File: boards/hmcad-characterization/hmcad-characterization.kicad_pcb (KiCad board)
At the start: 4 copper layers, 50 parts, among them J1 BARREL, J10 SMA, J11 SMA, J12 CONN_INTEGRALSTICK_FPGA_HOST, J2 SMA, J3 SMA, J4 SMA, J5 SMA, J6 SMA, J7 SMA, J8 SMA, J9 SMA, U1 ASG2-D-X-A-1000.000MHZ, U2 SIT9122AI-2D3-33E625.000000T, U3 PI6C59S6005, U4 LT3042, U5 HMCAD1520

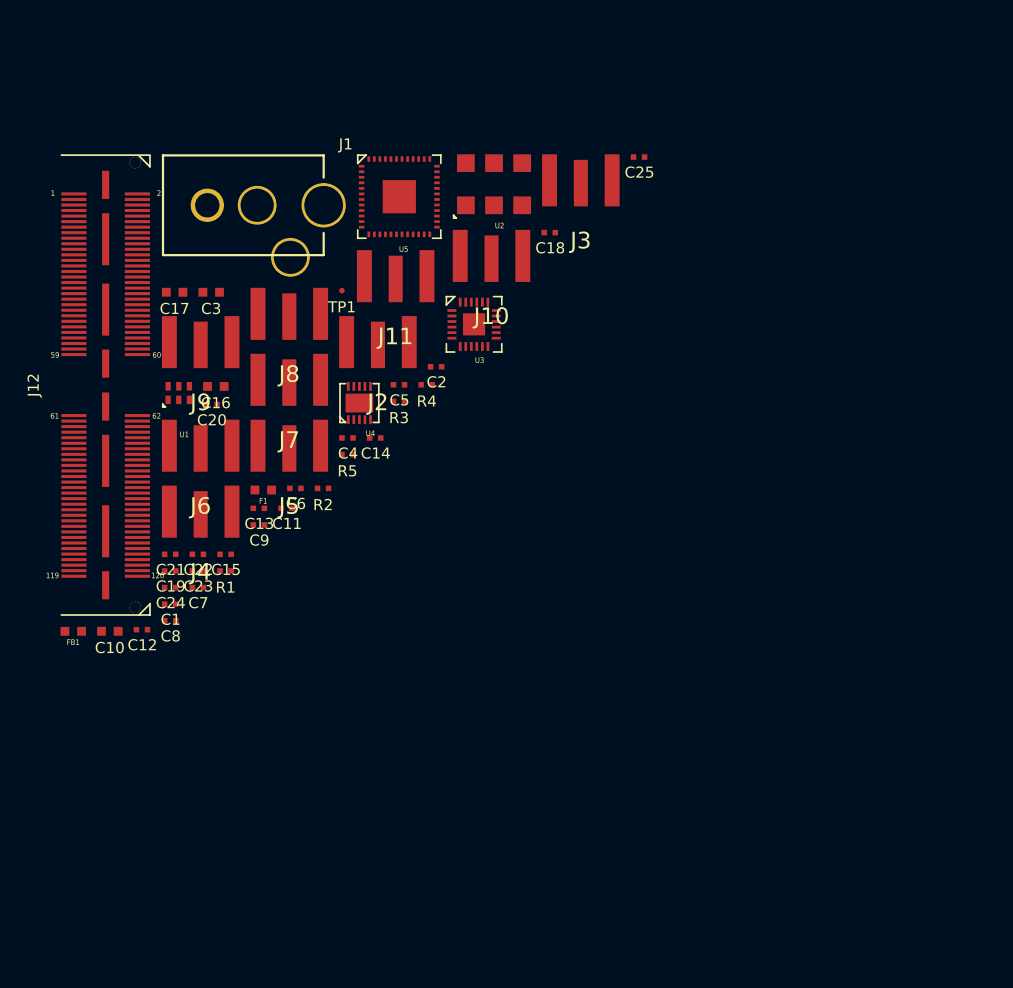
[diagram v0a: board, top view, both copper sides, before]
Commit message: Preliminary layout. Still have to do low speed control lines, power/ground planes, and transitions at SMAs.
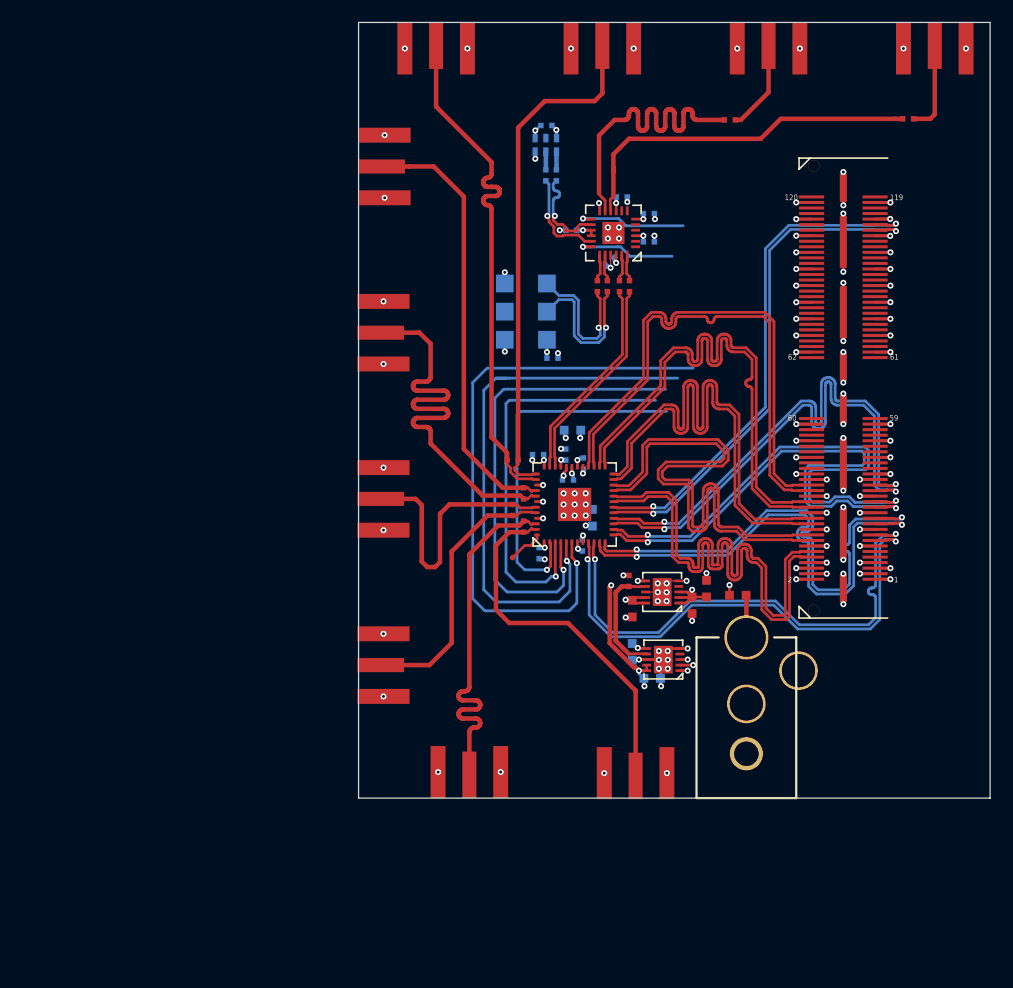
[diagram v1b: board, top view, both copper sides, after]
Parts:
- added C26: 4.7 uF, azonenberg_pcb:EIA_0603_CAP_NOSILK, B.Cu at (103.7, 86.8)
- added C27: 4.7 uF, azonenberg_pcb:EIA_0603_CAP_NOSILK, B.Cu at (105.5, 89.2)
- added U6: LT3042, azonenberg_pcb:DFN_10_0.5MM_3x3MM, F.Cu at (106.5, 87.5)
- C1, C15, C16, C17, C18, C19, C2, C20, C21, C22, C23, C24, C25, C4, C5, C6, C9, U1, U2: moved to B.Cu
- R1: value 33K 1% -> 9.09K 0.1%
- moved C13 68.3 mm to (128.6, 38.7), turned to 180 degrees
- moved J12 66.6 mm to (122.8, 63.0), turned to 180 degrees
- moved J1 63.7 mm to (114.0, 92.0), turned to 90 degrees
- moved FB1 57.3 mm to (110.4, 81.1), turned to 90 degrees
- moved C1 54.9 mm to (96.0, 39.3)
- moved J3 54.3 mm to (89.0, 100.0)
- moved C12 53.8 mm to (103.5, 53.8), turned to 90 degrees
- moved C3 51.8 mm to (109.1, 82.6), turned to 90 degrees
- moved C15 49.0 mm to (105.2, 47.2)
- moved C8 49.0 mm to (100.5, 53.8), turned to 270 degrees
- moved J9 47.8 mm to (101.0, 30.0), turned to 180 degrees
- moved C21 47.7 mm to (101.7, 51.6), turned to 225 degrees
- moved C10 47.2 mm to (103.7, 82.9), turned to 90 degrees
- moved J10 46.4 mm to (131.0, 30.0), turned to 180 degrees
- moved C7 45.9 mm to (101.5, 53.8), turned to 270 degrees
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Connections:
- net Net-(C11-Pad2) renamed /ADC_AC_P
- net Net-(C12-Pad2) renamed /ADC_AC_N
- net Net-(C13-Pad2) renamed /DEBUG_AC_P
- net Net-(C14-Pad2) renamed /DEBUG_AC_N
- net Net-(R1-Pad1) renamed /RSET
- C3 pad 2: Net-(C3-Pad2) -> /3V3_1
- C5 pad 1: /CLK_1GHZ_AC_P -> /CLK_1GHZ_AC_N
- C6 pad 1: /CLK_1GHZ_AC_N -> /CLK_1GHZ_AC_P
- C7 pad 2: /CLK_625MHZ_P -> /CLK_625MHZ_N
- C8 pad 2: /CLK_625MHZ_N -> /CLK_625MHZ_P
- FB1 pad 1: Net-(C3-Pad2) -> /3V3_1
- J12 pad 10: /FCLK_N -> /FCLK_P
- J12 pad 12: /FCLK_P -> /FCLK_N
- J12 pad 15: /LVDS_4B_N -> /LVDS_1A_P
- J12 pad 16: /LVDS_4A_N -> /LVDS_3A_P
- J12 pad 17: /LVDS_4B_P -> /LVDS_1A_N
- J12 pad 18: /LVDS_4A_P -> /LVDS_3A_N
- J12 pad 21: /LVDS_3B_N -> /LVDS_1B_P
- J12 pad 22: /LVDS_3A_N -> /LVDS_3B_P
- J12 pad 23: /LVDS_3B_P -> /LVDS_1B_N
- J12 pad 24: /LVDS_3A_P -> /LVDS_3B_N
- J12 pad 27: /LVDS_2B_N -> /LVDS_2A_P
- J12 pad 28: /LVDS_2A_N -> /LVDS_4A_P
- J12 pad 29: /LVDS_2B_P -> /LVDS_2A_N
- J12 pad 30: /LVDS_2A_P -> /LVDS_4A_N
- J12 pad 33: /LVDS_1B_N -> /LVDS_2B_P
- J12 pad 34: /LVDS_1A_N -> /LVDS_4B_P
- J12 pad 35: /LVDS_1B_P -> /LVDS_2B_N
- J12 pad 36: /LVDS_1A_P -> /LVDS_4B_N
- U4 pad 1: Net-(C3-Pad2) -> /3V3_1
- U4 pad 2: Net-(C3-Pad2) -> /3V3_1
- U4 pad 3: Net-(C3-Pad2) -> /3V3_1
- U4 pad 6: /3V3 -> /3V3_1
- U5 pad PAD: (no net) -> /GND
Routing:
- net /GND: track 0.00 -> 500.9 mm, vias 0 -> 86
- net /3V3: track 0.00 -> 171.9 mm, vias 0 -> 28
- net /1V8: track 0.00 -> 93.9 mm, vias 0 -> 14
- net /ADC_PD: track 0.00 -> 55.8 mm, vias 0 -> 1
- net /A1V8: track 0.00 -> 55.6 mm, vias 0 -> 8
- net /ADC_RST_N: track 0.00 -> 50.1 mm, vias 0 -> 1
- net /IN4_P: track 0.00 -> 47.1 mm
- net /LVDS_2A_N: track 0.00 -> 46.8 mm, vias 0 -> 2
- net /LVDS_4B_P: track 0.00 -> 46.7 mm
- net /LVDS_2A_P: track 0.00 -> 46.7 mm, vias 0 -> 2
- net /LVDS_4A_P: track 0.00 -> 46.7 mm
- net /LCLK_P: track 0.00 -> 46.7 mm, vias 0 -> 2
- net /LCLK_N: track 0.00 -> 46.7 mm, vias 0 -> 2
- net /LVDS_4B_N: track 0.00 -> 46.7 mm
- net /FCLK_N: track 0.00 -> 46.7 mm
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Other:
- board outline added: 57 x 70 mm

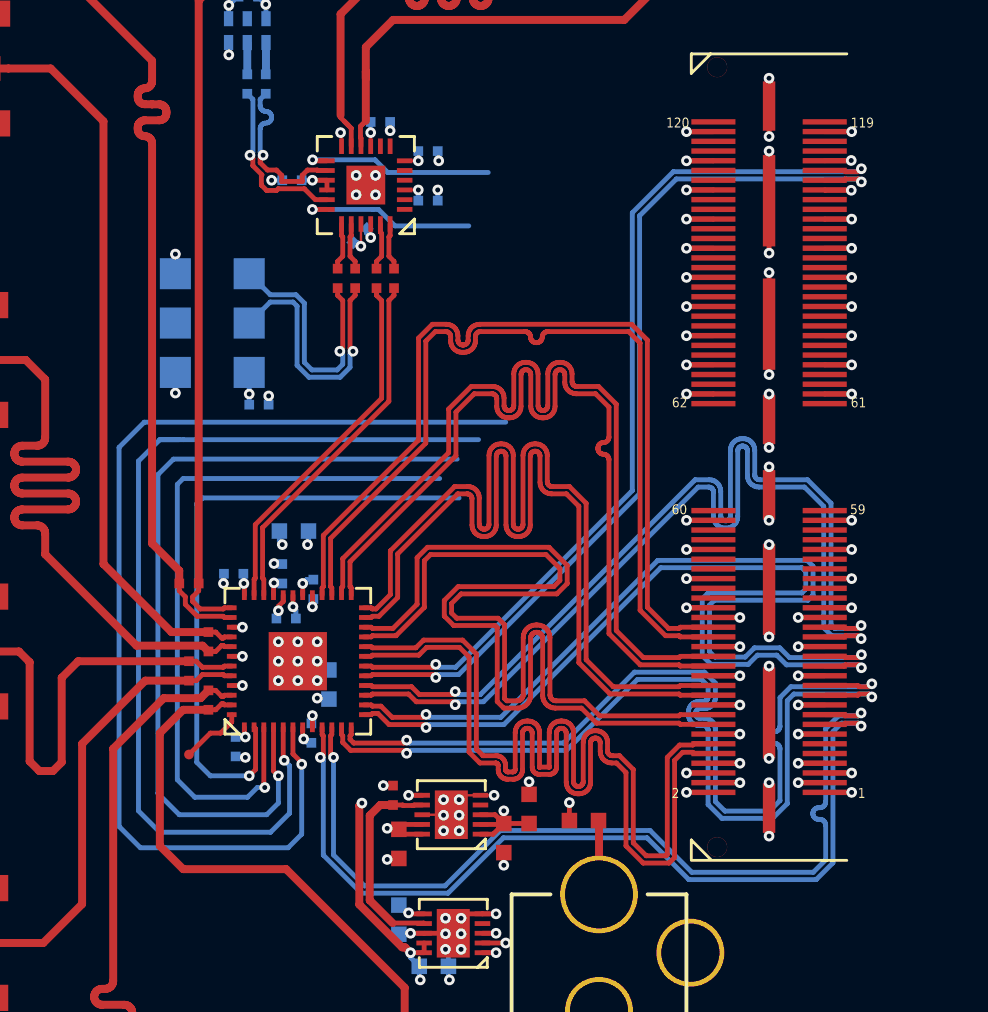
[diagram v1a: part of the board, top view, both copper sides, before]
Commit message: Continued layout on ADC test board. Fixed a bunch of plane crossings.
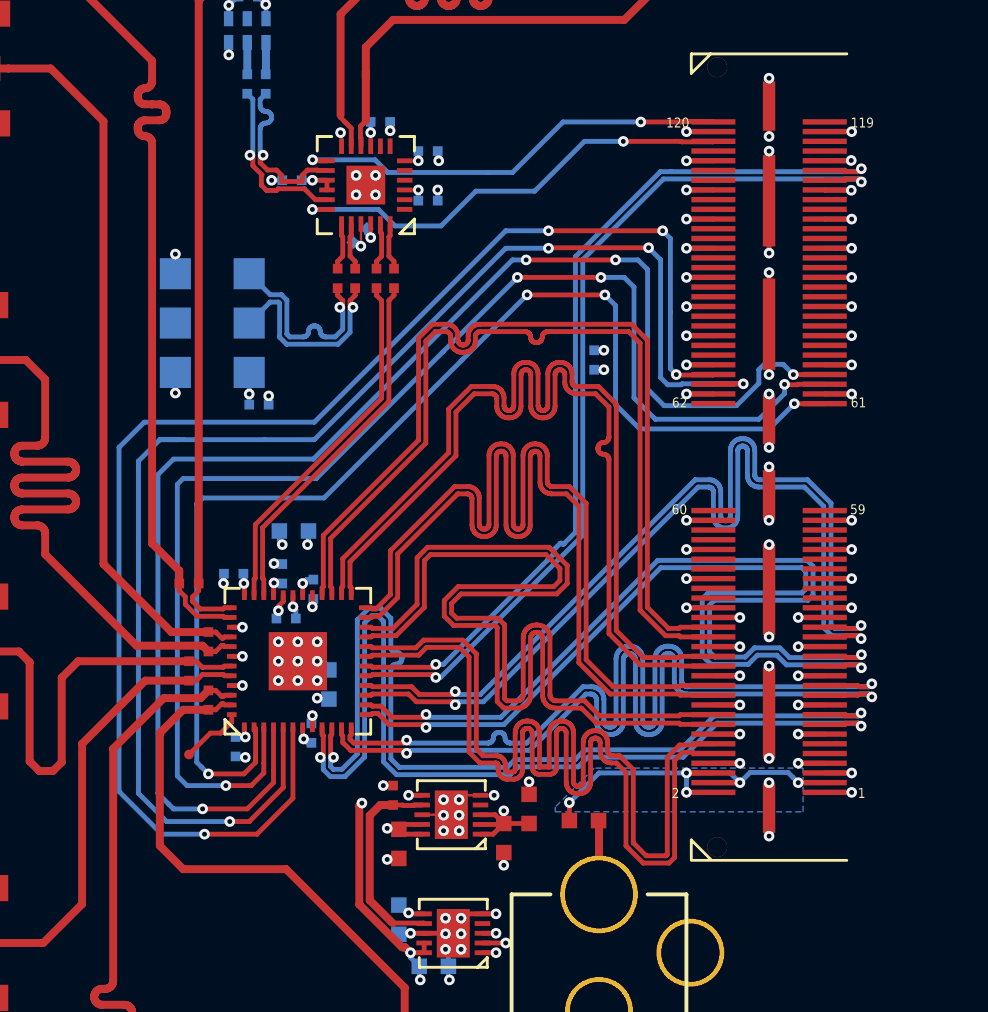
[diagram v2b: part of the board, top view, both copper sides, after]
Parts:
- added C28: 0.47 uF, azonenberg_pcb:EIA_0402_CAP_NOSILK, B.Cu at (113.8, 58.0)
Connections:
- J12 pad 116: (no net) -> /BUF_MUXSEL
- J12 pad 120: (no net) -> /BUF_IN_SEL
- J12 pad 61: (no net) -> /SPI_CS_N
- J12 pad 62: /ADC_PD -> (no net)
- J12 pad 65: /ADC_RST_N -> /SPI_SDATA
- J12 pad 66: /SPI_SCLK -> /ADC_RST_N
- J12 pad 67: /SPI_SDATA -> /SPI_SCLK
- J12 pad 68: /SPI_CS_N -> /ADC_PD
- J12 pad 73: /BUF_MUXSEL -> (no net)
- J12 pad 74: /BUF_IN_SEL -> (no net)
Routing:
- net /SPI_SDATA: track 37.0 -> 67.4 mm, vias 1 -> 4
- net /SPI_SCLK: track 43.0 -> 73.2 mm, vias 1 -> 4
- net /SPI_CS_N: track 32.6 -> 61.8 mm, vias 1 -> 4
- net /ADC_RST_N: track 50.1 -> 73.7 mm, vias 1 -> 4
- net /ADC_PD: track 55.8 -> 74.2 mm, vias 1 -> 4
- net /3V3: track 171.9 -> 187.3 mm, vias 28 -> 29
- net /BUF_MUXSEL: track 9.15 -> 23.6 mm, vias 1 -> 2
- net /BUF_IN_SEL: track 10.1 -> 22.8 mm, vias 1 -> 2
- net /A1V8: track 55.6 -> 51.9 mm
- net /CLK_625MHZ_N: track 13.5 -> 10.3 mm
- net /CLK_625MHZ_P: track 12.9 -> 10.3 mm
- net /LVDS_1A_P: track 46.6 -> 48.6 mm
- net /LVDS_1A_N: track 46.7 -> 48.5 mm
- net /1V8: track 93.9 -> 92.5 mm, vias 14 -> 15
- net /5V0: track 27.9 -> 27.2 mm
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- added copper zone on In2.Cu, net /1V8
- added copper zone on In2.Cu, net /2V5
- added copper zone on In2.Cu, net /3V3
- added copper zone on In2.Cu, net /3V3_1
- added copper zone on B.Cu, net /5V0
- added copper zone on In2.Cu, net /5V0
- added copper zone on In2.Cu, net /A1V8
- added copper zone on In1.Cu, net /GND

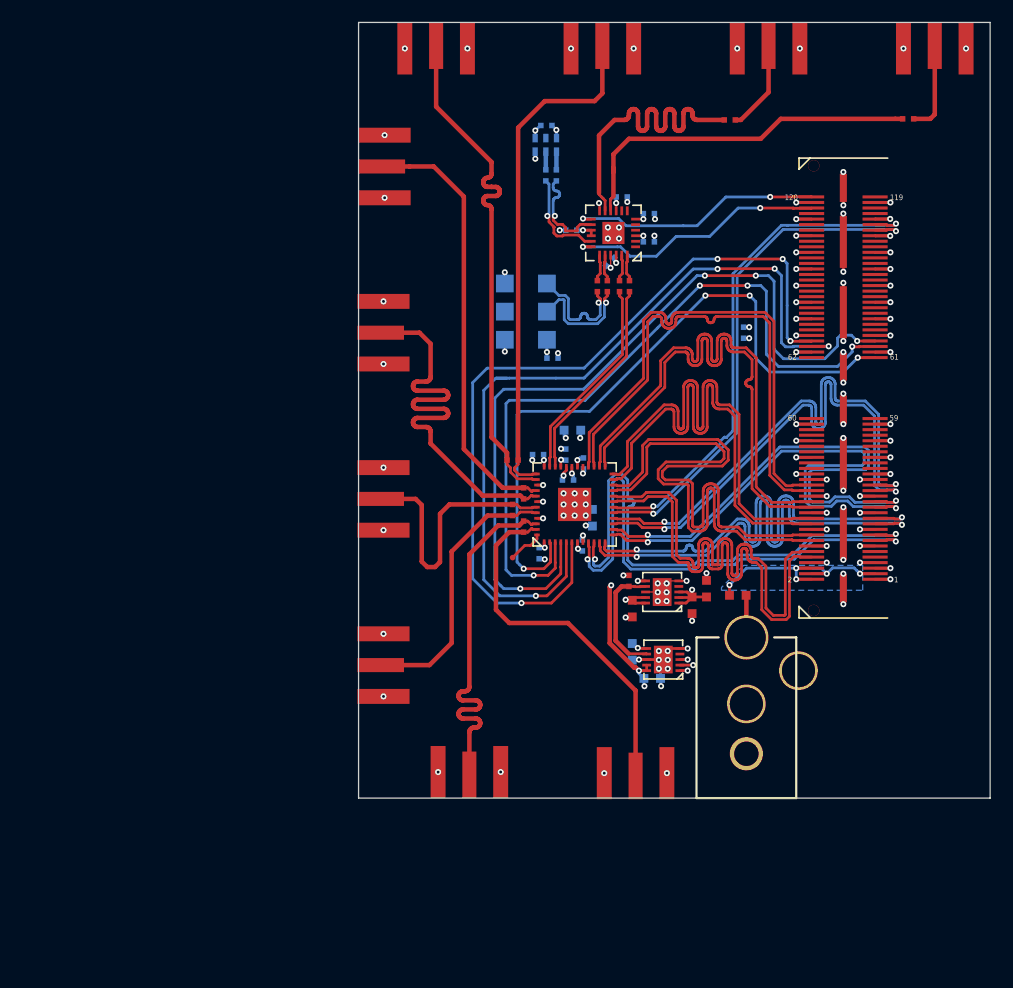
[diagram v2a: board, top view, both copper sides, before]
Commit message: Additional routing tweaks, added soldermask cutouts over RF traces
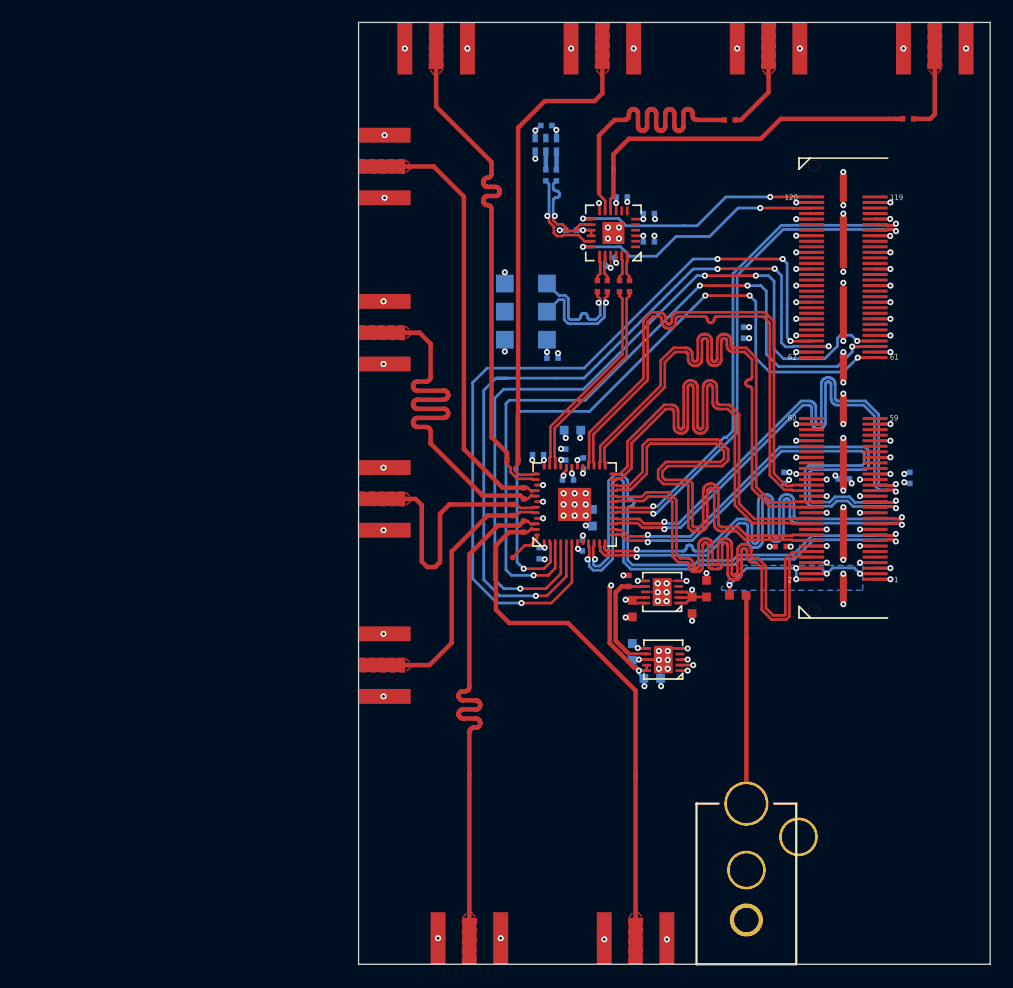
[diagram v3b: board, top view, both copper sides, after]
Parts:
- added C29: 0.47 uF, azonenberg_pcb:EIA_0402_CAP_NOSILK, B.Cu at (117.4, 71.1)
- added C30: 0.47 uF, azonenberg_pcb:EIA_0402_CAP_NOSILK, B.Cu at (122.8, 71.2)
- added C31: 0.47 uF, azonenberg_pcb:EIA_0402_CAP_NOSILK, B.Cu at (128.8, 71.1)
- added C32: 0.47 uF, azonenberg_pcb:EIA_0402_CAP_NOSILK, F.Cu at (117.1, 77.3)
- moved J1 15.0 mm to (114.0, 107.0)
- moved J3 15.0 mm to (89.0, 115.0)
- moved J2 14.9 mm to (104.0, 115.0)
- moved J4 0.10 mm to (79.0, 88.0)
- moved J5 0.10 mm to (79.0, 73.0)
- moved J6 0.10 mm to (79.0, 58.0)
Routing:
- net /GND: track 500.9 -> 561.2 mm
- net /1V8: track 92.5 -> 107.9 mm, vias 15 -> 19
- net Net-(F1-Pad1): track 3.75 -> 18.8 mm
- net /IN1_N: track 33.5 -> 48.5 mm
- net /IN1_P: track 33.5 -> 48.4 mm
- net /2V5: track 34.4 -> 47.5 mm, vias 12 -> 16
- net /3V3: track 187.3 -> 188.9 mm
- added copper zone on F.Cu, net /DEBUG_CLK_N
- added copper zone on F.Cu, net /DEBUG_CLK_P
- added copper zone on F.Cu, net /IN1_N
- added copper zone on F.Cu, net /IN1_P
- added copper zone on F.Cu, net /IN2_N
- added copper zone on F.Cu, net /IN2_P
- added copper zone on F.Cu, net /IN3_N
- added copper zone on F.Cu, net /IN3_P
- added copper zone on F.Cu, net /IN4_N
- added copper zone on F.Cu, net /IN4_P
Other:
- board size 57 x 70 mm -> 57 x 85 mm

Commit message: Final hmcad-characterization board as sent to fab
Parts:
- added G***: LOGO, azonenberg_pcb:LONGTHING-1200DPI, F.Cu at (125.5, 110.0)
- added G***: LOGO, w_logo:Logo_silk_ROHS_5x2.8mm, F.Cu at (130.5, 107.5)
- added G***: LOGO, w_logo:Logo_silk_WEEE_3.4x5mm, F.Cu at (130.5, 102.0)
- added G***: LOGO, w_logo:Logo_silk_OSHW_6x6mm, F.Cu at (124.0, 101.5)
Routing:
- net /DEBUG_AC_N: track 30.1 -> 33.1 mm
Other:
- rule solder_mask_min_width: 0.25 -> 0.05
- board text added: "HMCAD1520 Testbed A. Zonenberg / v0.1 2020-04-04"
